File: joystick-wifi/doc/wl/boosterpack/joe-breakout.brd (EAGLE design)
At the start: 6 parts, among them J10 FE04-2, J2 FE04-2

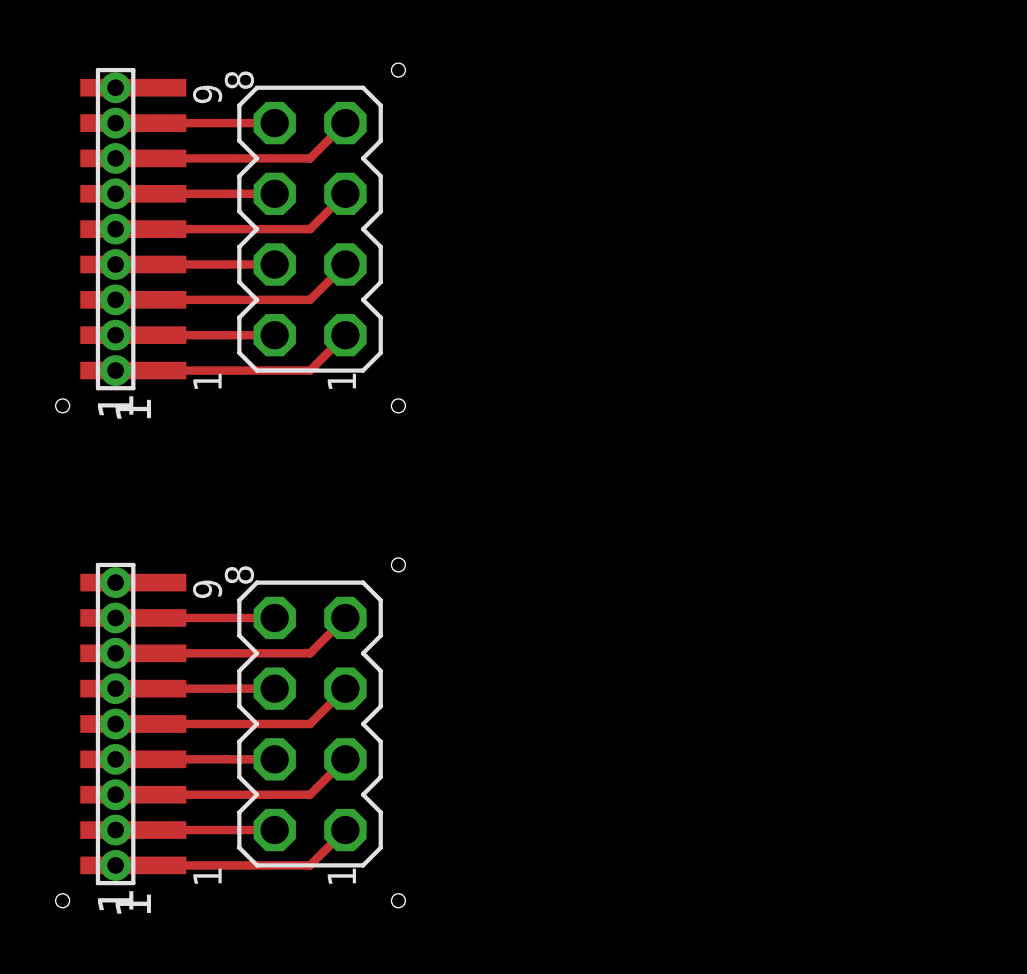
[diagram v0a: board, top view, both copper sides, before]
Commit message: cc2500: improve cc2500 breakout PCB
Arrange two same PCBs horizontally (instead of vertical layout)
so that it can be printed with economy of PCB tape.

Signed-off-by: Sam Protsenko <joe.skb7@gmail.com>
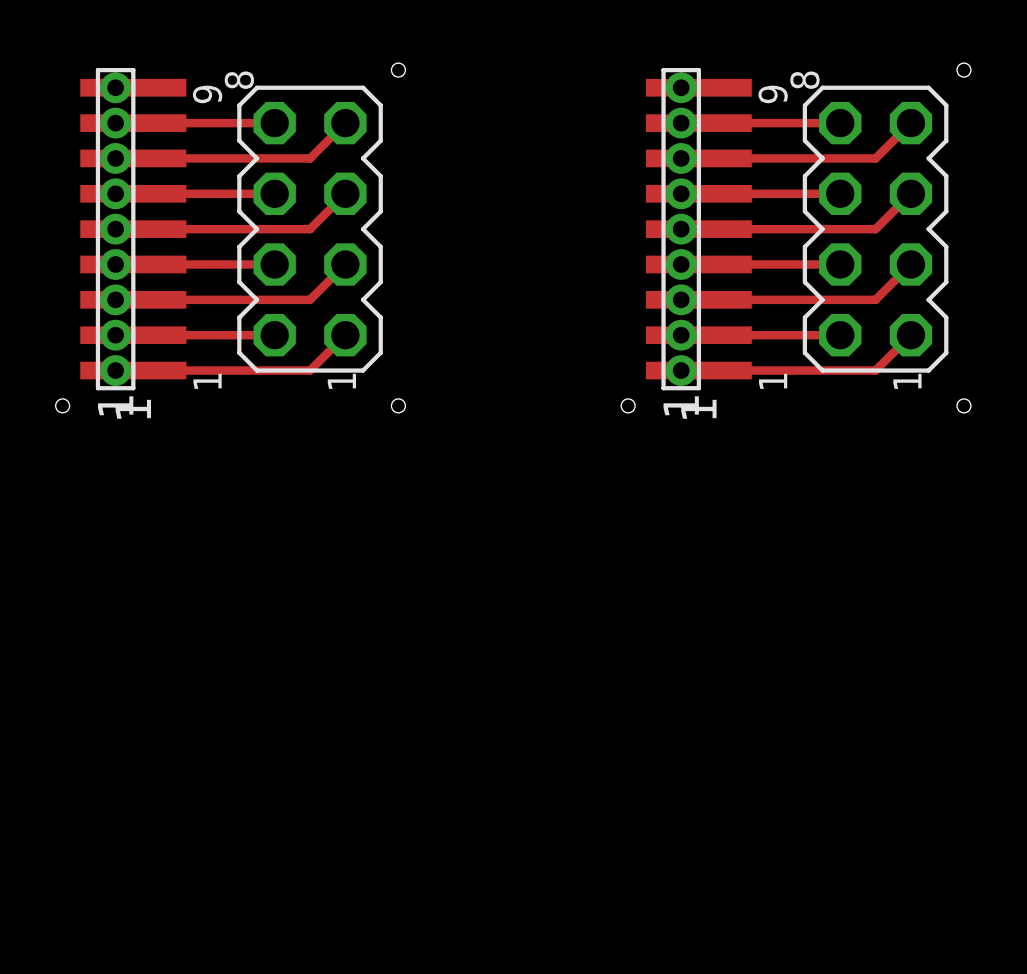
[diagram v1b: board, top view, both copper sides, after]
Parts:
- moved J1 27.0 mm to (48.9, 43.8)
- moved J2 27.0 mm to (55.2, 43.8)
- moved J4 27.0 mm to (48.3, 43.8)
